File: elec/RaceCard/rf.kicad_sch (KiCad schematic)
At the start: 0 parts

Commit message: Ajout du schéma pour TX
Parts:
- added AE1: Antenna_Loop, symbol Device:Antenna_Loop
- added C1, C2: 18pF, Capacitor_SMD:C_0603_1608Metric, symbol Device:C_Small
- added C3: 100pF, Capacitor_SMD:C_0603_1608Metric, symbol Device:C_Small
- added C4: 10pF, Capacitor_SMD:C_0603_1608Metric, symbol Device:C_Small
- added C5: 10uF, Capacitor_SMD:C_0603_1608Metric, symbol Device:C_Small
- added C6: 0.1uF, Capacitor_SMD:C_0603_1608Metric, symbol Device:C_Small
- added C7: 3.9pF, Capacitor_SMD:C_0603_1608Metric, symbol Device:C_Small
- added L1: 470nH, Inductor_SMD:L_0603_1608Metric, symbol Device:L_Small
- added L2: 82nH, Inductor_SMD:L_0603_1608Metric, symbol Device:L_Small
- added R1: 0, Resistor_SMD:R_0603_1608Metric, symbol Device:R_Small_US
- added U1: MICRF112YMM, MSOP10_MC_MCH, symbol C3I_A25:MICRF112YMM
- added Y1: 13.560MHZ, ABLS-13.560MHZ-10-R20-D-T:XTAL_ABLS-13.560MHZ-10-R20-D-T, symbol C3I_A25:ABLS-13.560MHZ-10-R20-D-T
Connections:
- new net: C4.1, L1.2, U1.9 (PAOUT)
- new net: C4.2, L2.1
- new net: AE1.1, C7.2, L2.2
- new net: C2.2, U1.3 (XTLOUT), Y1.1
- new net: C1.2, U1.2 (XTLIN), Y1.2
- new net: L1.1, R1.2
- new net DATA: U1.1 (ASK)
- new net GND: AE1.2, C1.1, C2.1, C3.1, C3.2, C5.1, C5.2, C6.1, C6.2, C7.1, R1.1, U1.10 (VDD), U1.4 (VSS), U1.8 (VSSPA)
- new net VDD: U1.5 (XTAL_MOD), U1.6 (FSK), U1.7 (EN)

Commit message: Commence plugger choses
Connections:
- net GND: no longer C3.2, C5.2, C6.2, R1.1, U1.10 (VDD)
- net VDD: now also C3.2, C5.2, C6.2, R1.1, U1.10 (VDD)
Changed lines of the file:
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@@
+	)
+	(junction
+		(at 173.99 97.79)
+		(diameter 0)
+		(color 0 0 0 0)
+	)
+	(junction
+		(at 191.77 85.09)
+		(diameter 0)
+		(color 0 0 0 0)
+	)
+	(junction
+		(at 200.66 85.09)
+		(diameter 0)
+		(color 0 0 0 0)
+	)
+	(junction
+		(at 85.09 100.33)
+		(diameter 0)
+		(color 0 0 0 0)
+	)
+	(junction
+		(at 200.66 97.79)
+		(diameter 0)
+		(color 0 0 0 0)
+	)
+	(junction
+		(at 177.8 102.87)
+		(diameter 0)
+		(color 0 0 0 0)
+	)
+	(junction
+		(at 100.33 87.63)
+		(diameter 0)
+		(color 0 0 0 0)
 	)
 	(junction
@@
 	)
 	(junction
-		(at 173.99 97.79)
-		(diameter 0)
-		(color 0 0 0 0)
-	)
-	(junction
-		(at 191.77 85.09)
-		(diameter 0)
-		(color 0 0 0 0)
-	)
-	(junction
-		(at 200.66 85.09)
-		(diameter 0)
-		(color 0 0 0 0)
-	)
-	(junction
-		(at 85.09 100.33)
-		(diameter 0)
-		(color 0 0 0 0)
-	)
-	(junction
-		(at 200.66 97.79)
-		(diameter 0)
-		(color 0 0 0 0)
-	)
-	(junction
-		(at 177.8 102.87)
-		(diameter 0)
-		(color 0 0 0 0)
-	)
-	(junction
-		(at 100.33 87.63)
-		(diameter 0)
-		(color 0 0 0 0)
-	)
-	(junction
 		(at 191.77 77.47)
 		(diameter 0)
@@
 	(wire
 		(pts
+			(xy 200.66 77.47) (xy 208.28 77.47)
+		)
+		(stroke
+			(width 0)
+			(type default)
+		)
+	)
+	(wire
+		(pts
 			(xy 170.18 77.47) (xy 173.99 77.47)
 		)
@@
 		(pts
 			(xy 182.88 97.79) (xy 173.99 97.79)
-		)
-		(stroke
-			(width 0)
-			(type default)
-		)
-	)
-	(wire
-		(pts
-			(xy 200.66 74.93) (xy 200.66 77.47)
 		)
 		(stroke
@@
 				(hide yes)
 			)
+		)
+	)
+	(hierarchical_label "VDD"
+		(shape input)
+		(at 208.28 77.47 0)
+		(effects
+			(font
+				(size 1.27 1.27)
+			)
+			(justify left)
 		)
 	)
@@
 					(unit 1)
 				)
-			)
-		)
-	)
-	(symbol
-		(lib_id "power:GND")
-		(at 200.66 74.93 180)
-		(unit 1)
-		(exclude_from_sim no)
-		(in_bom yes)
-		(on_board yes)
-		(dnp no)
-		(fields_autoplaced yes)
-		(property "Reference" "#PWR0103"
-			(at 200.66 68.58 0)
-			(effects
-				(font
-					(size 1.27 1.27)
-				)
-				(hide yes)
-			)
-		)
-		(property "Value" "GND"
-			(at 200.66 69.85 0)
-			(effects
-				(font
-					(size 1.27 1.27)
-				)
-				(hide yes)
-			)
-		)
-		(property "Footprint" ""
-			(at 200.66 74.93 0)
-			(effects
-				(font
-					(size 1.27 1.27)
-				)
-				(hide yes)
-			)
-		)
-		(property "Datasheet" ""
-			(at 200.66 74.93 0)
-			(effects
-				(font
-					(size 1.27 1.27)
-				)
-				(hide yes)
-			)
-		)
-		(property "Description" "Power symbol creates a global label with name \"GND\" , ground"
-			(at 200.66 74.93 0)
-			(effects
-				(font
-					(size 1.27 1.27)
-				)
-				(hide yes)
-			)
-		)
-		(pin "1"
-		)
-		(instances
-			(project "rf"
-				(path "/b088a105-323b-4bb6-85e9-cf97c58d108d"
-					(reference "#PWR08")
-					(unit 1)
-				)
-			)
-			(project "RaceCard"
-				(path "/fef6ab1d-cc84-41bb-aff7-8da28fd37bf7/00fed2a2-695a-48f3-8dd8-7873b3152cc9"
-					(reference "#PWR0103")
-					(unit 1)
-				)

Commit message: Modif
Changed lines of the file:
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@@
+	(wire
+		(pts
+			(xy 116.84 95.25) (xy 118.11 95.25)
+		)
+		(stroke
+			(width 0)
+			(type default)
+		)
+	)
 	(wire
 		(pts
@@
 		)
 	)
-	(global_label "DATA"
-		(shape input)
-		(at 118.11 95.25 180)
-		(fields_autoplaced yes)
-		(effects
-			(font
-				(size 1.27 1.27)
-			)
-			(justify right)
-		)
-		(property "Intersheetrefs" "${INTERSHEET_REFS}"
-			(at 110.71 95.25 0)
-			(effects
-				(font
-					(size 1.27 1.27)
-				)
-				(justify right)
-				(hide yes)
-			)
-		)
-	)
 	(hierarchical_label "VDD"
 		(shape input)
@@
 		)
 	)
+	(hierarchical_label "DATA"
+		(shape input)
+		(at 116.84 95.25 180)
+		(effects
+			(font
+				(size 1.27 1.27)
+			)
+			(justify right)
+		)
+	)

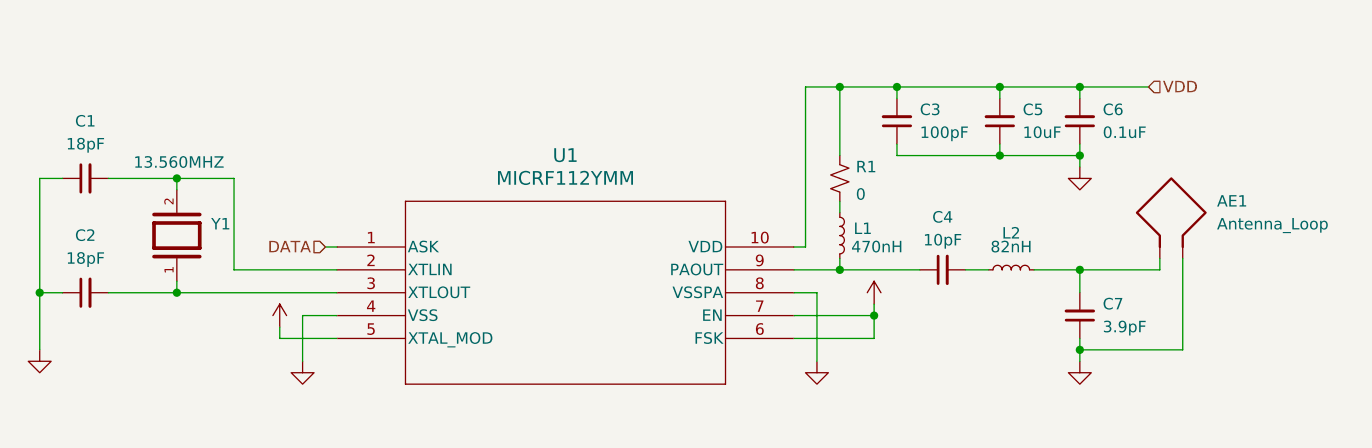
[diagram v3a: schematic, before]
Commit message: ajout connecteur usb c et leds
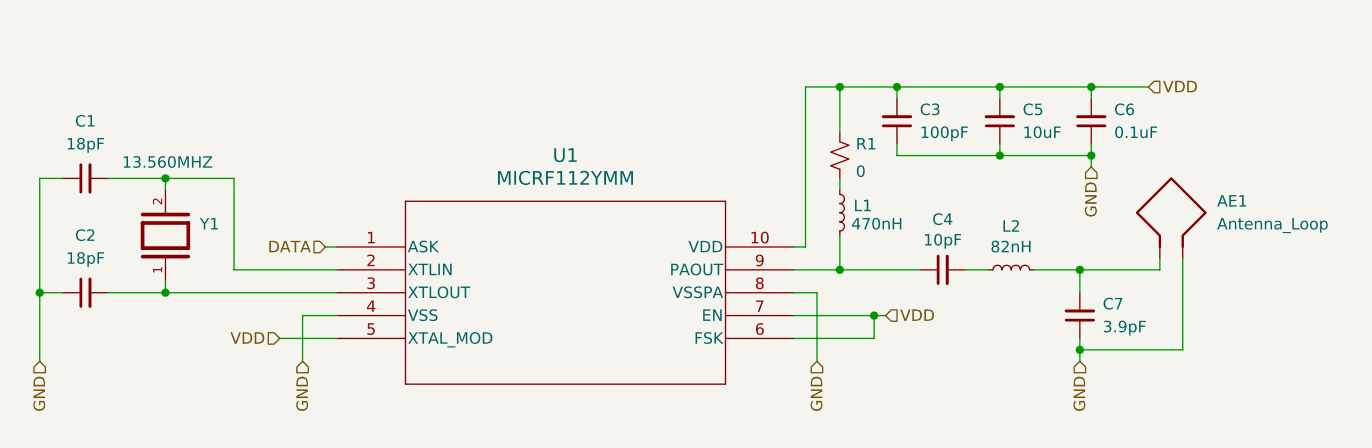
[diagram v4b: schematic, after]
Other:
- moved on the sheet: C6, L1, R1, Y1

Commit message: + test points
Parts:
- added TP7: VDD, TestPoint:TestPoint_THTPad_3.0x3.0mm_Drill1.5mm, symbol Connector:TestPoint
- renumbered C3 to C21, C5 to C22, C6 to C23, C1 to C24, C4 to C25, C2 to C26, C7 to C27, R1 to R19, U1 to U6
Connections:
- net VDD: now also TP7.1
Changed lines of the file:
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@@
+	(wire
+		(pts
+			(xy 173.99 76.2) (xy 173.99 77.47)
+		)
+		(stroke
+			(width 0)
+			(type default)
+		)
+	)
 	(wire
 		(pts
@@
 		(on_board yes)
 		(dnp no)
-		(property "Reference" "C4"
+		(property "Reference" "C25"
 			(at 185.42 92.202 90)
 			(effects
@@
 			(project "RaceCard"
 				(path "/fef6ab1d-cc84-41bb-aff7-8da28fd37bf7/00fed2a2-695a-48f3-8dd8-7873b3152cc9"
-					(reference "C4")
+					(reference "C25")
 					(unit 1)
 				)
@@
 		(dnp no)
 		(fields_autoplaced yes)
-		(property "Reference" "C3"
+		(property "Reference" "C21"
 			(at 182.88 80.0035 0)
 			(effects
@@
 			(project "RaceCard"
 				(path "/fef6ab1d-cc84-41bb-aff7-8da28fd37bf7/00fed2a2-695a-48f3-8dd8-7873b3152cc9"
-					(reference "C3")
+					(reference "C21")
 					(unit 1)
 				)
@@
 		(dnp no)
 		(fields_autoplaced yes)
-		(property "Reference" "C5"
+		(property "Reference" "C22"
 			(at 194.31 80.0035 0)
 			(effects
@@
 			(project "RaceCard"
 				(path "/fef6ab1d-cc84-41bb-aff7-8da28fd37bf7/00fed2a2-695a-48f3-8dd8-7873b3152cc9"
-					(reference "C5")
+					(reference "C22")
 					(unit 1)
 				)
@@
 		(dnp no)
 		(fields_autoplaced yes)
-		(property "Reference" "C2"
+		(property "Reference" "C26"
 			(at 90.1763 93.98 90)
 			(effects
@@
 			(project "RaceCard"
 				(path "/fef6ab1d-cc84-41bb-aff7-8da28fd37bf7/00fed2a2-695a-48f3-8dd8-7873b3152cc9"
-					(reference "C2")
+					(reference "C26")
+					(unit 1)
+				)
+			)
+		)
+	)
+	(symbol
+		(lib_id "Connector:TestPoint")
+		(at 173.99 76.2 0)
+		(unit 1)
+		(exclude_from_sim no)
+		(in_bom yes)
+		(on_board yes)
+		(dnp no)
+		(fields_autoplaced yes)
+		(property "Reference" "TP7"
+			(at 176.53 71.6279 0)
+			(effects
+				(font
+					(size 1.27 1.27)
+				)
+				(justify left)
+			)
+		)
+		(property "Value" "VDD"
+			(at 176.53 74.1679 0)
+			(effects
+				(font
+					(size 1.27 1.27)
+				)
+				(justify left)
+			)
+		)
+		(property "Footprint" "TestPoint:TestPoint_THTPad_3.0x3.0mm_Drill1.5mm"
+			(at 179.07 76.2 0)
+			(effects
+				(font
+					(size 1.27 1.27)
+				)
+				(hide yes)
+			)
+		)
+		(property "Datasheet" "~"
+			(at 179.07 76.2 0)
+			(effects
+				(font
+					(size 1.27 1.27)
+				)
+				(hide yes)
+			)
+		)
+		(property "Description" "test point"
+			(at 173.99 76.2 0)
+			(effects
+				(font
+					(size 1.27 1.27)
+				)
+				(hide yes)
+			)
+		)
+		(pin "1"
+		)
+		(instances
+			(project "RaceCard"
+				(path "/fef6ab1d-cc84-41bb-aff7-8da28fd37bf7/00fed2a2-695a-48f3-8dd8-7873b3152cc9"
+					(reference "TP7")
 					(unit 1)
 				)
@@
 		(dnp no)
 		(fields_autoplaced yes)
-		(property "Reference" "U1"
+		(property "Reference" "U6"
 			(at 143.51 85.09 0)
 			(effects
@@
 			(project ""
 				(path "/fef6ab1d-cc84-41bb-aff7-8da28fd37bf7/00fed2a2-695a-48f3-8dd8-7873b3152cc9"
-					(reference "U1")
+					(reference "U6")
 					(unit 1)
 				)
@@
 		(dnp no)
 		(fields_autoplaced yes)
-		(property "Reference" "C6"
+		(property "Reference" "C23"
 			(at 204.47 80.0035 0)
 			(effects
@@
 			(project "RaceCard"
 				(path "/fef6ab1d-cc84-41bb-aff7-8da28fd37bf7/00fed2a2-695a-48f3-8dd8-7873b3152cc9"
-					(reference "C6")
+					(reference "C23")
 					(unit 1)
 				)
@@
 		(dnp no)
 		(fields_autoplaced yes)
-		(property "Reference" "C1"
+		(property "Reference" "C24"
 			(at 90.1763 81.28 90)
 			(effects
@@
 			(project "RaceCard"
 				(path "/fef6ab1d-cc84-41bb-aff7-8da28fd37bf7/00fed2a2-695a-48f3-8dd8-7873b3152cc9"
-					(reference "C1")
+					(reference "C24")
 					(unit 1)
 				)
@@
 		(on_board yes)
 		(dnp no)
-		(property "Reference" "R1"
+		(property "Reference" "R19"
 			(at 175.768 83.82 0)
 			(effects
@@
 			(project "RaceCard"
 				(path "/fef6ab1d-cc84-41bb-aff7-8da28fd37bf7/00fed2a2-695a-48f3-8dd8-7873b3152cc9"
-					(reference "R1")
+					(reference "R19")
 					(unit 1)
 				)
@@
 		(dnp no)
 		(fields_autoplaced yes)
-		(property "Reference" "C7"
+		(property "Reference" "C27"
 			(at 203.2 101.5935 0)
 			(effects
@@
 			(project "RaceCard"
 				(path "/fef6ab1d-cc84-41bb-aff7-8da28fd37bf7/00fed2a2-695a-48f3-8dd8-7873b3152cc9"
-					(reference "C7")
-					(unit 1)
-				)
+					(reference "C27")
+					(unit 1)
+				)

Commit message: Fix des footprints et edge cuts
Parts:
- U6: footprint MSOP10_MC_MCH -> C3I:MSOP10_MC_MCH
- Y1: footprint ABLS-13.560MHZ-10-R20-D-T:XTAL_ABLS-13.560MHZ-10-R20-D-T -> C3I:XTAL_ABLS-13.560MHZ-10-R20-D-T
- renumbered R19 to R18, TP7 to TP16
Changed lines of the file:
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@@
 			)
 		)
-		(property "Footprint" "ABLS-13.560MHZ-10-R20-D-T:XTAL_ABLS-13.560MHZ-10-R20-D-T"
+		(property "Footprint" "C3I:XTAL_ABLS-13.560MHZ-10-R20-D-T"
 			(at 99.06 93.98 0)
 			(effects
@@
 		(dnp no)
 		(fields_autoplaced yes)
-		(property "Reference" "TP7"
+		(property "Reference" "TP16"
 			(at 176.53 71.6279 0)
 			(effects
@@
 			(project "RaceCard"
 				(path "/fef6ab1d-cc84-41bb-aff7-8da28fd37bf7/00fed2a2-695a-48f3-8dd8-7873b3152cc9"
-					(reference "TP7")
+					(reference "TP16")
 					(unit 1)
 				)
@@
 			)
 		)
-		(property "Footprint" "MSOP10_MC_MCH"
+		(property "Footprint" "C3I:MSOP10_MC_MCH"
 			(at 118.11 95.25 0)
 			(effects
@@
 		(on_board yes)
 		(dnp no)
-		(property "Reference" "R19"
+		(property "Reference" "R18"
 			(at 175.768 83.82 0)
 			(effects
@@
 			(project "RaceCard"
 				(path "/fef6ab1d-cc84-41bb-aff7-8da28fd37bf7/00fed2a2-695a-48f3-8dd8-7873b3152cc9"
-					(reference "R19")
-					(unit 1)
-				)
+					(reference "R18")
+					(unit 1)
+				)

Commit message: Power net update et cleanup sch
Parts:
- renumbered C21 to C23, C22 to C24, C23 to C25, C24 to C26, C25 to C27, C26 to C28, C27 to C29, R18 to R17, TP16 to TP17
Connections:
- net VDD renamed +3V3
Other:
- moved on the sheet: C29
